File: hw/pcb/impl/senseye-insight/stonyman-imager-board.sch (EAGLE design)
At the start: 10 parts, among them J1 HEADER_12PIN2X6_NOSILK, U1 STONYMANDEFAULT_LENS_MOUNT, U2 TI_ADCXX1S101

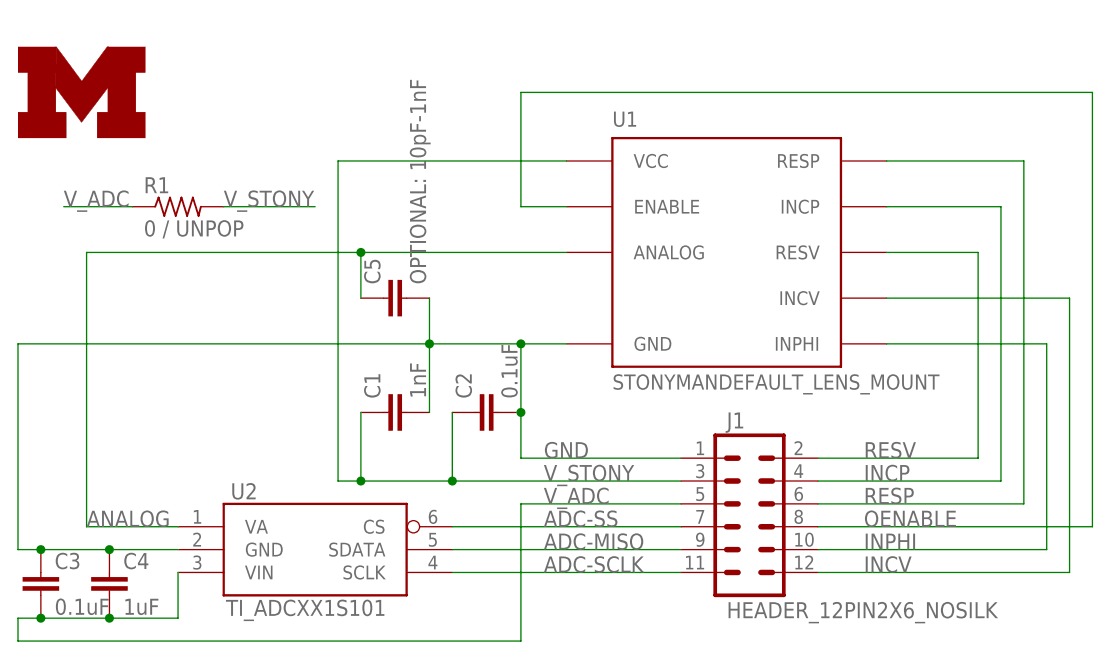
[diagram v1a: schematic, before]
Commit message: fixed ADC pin swap bug in stonyman-imager-board
I had switched pin 1 with pin 3, the positive supply and analog in pins
respectively, due to their stupid names.  I have updated the part so
that the names are very clear now, and also fixed the schematic and
board.
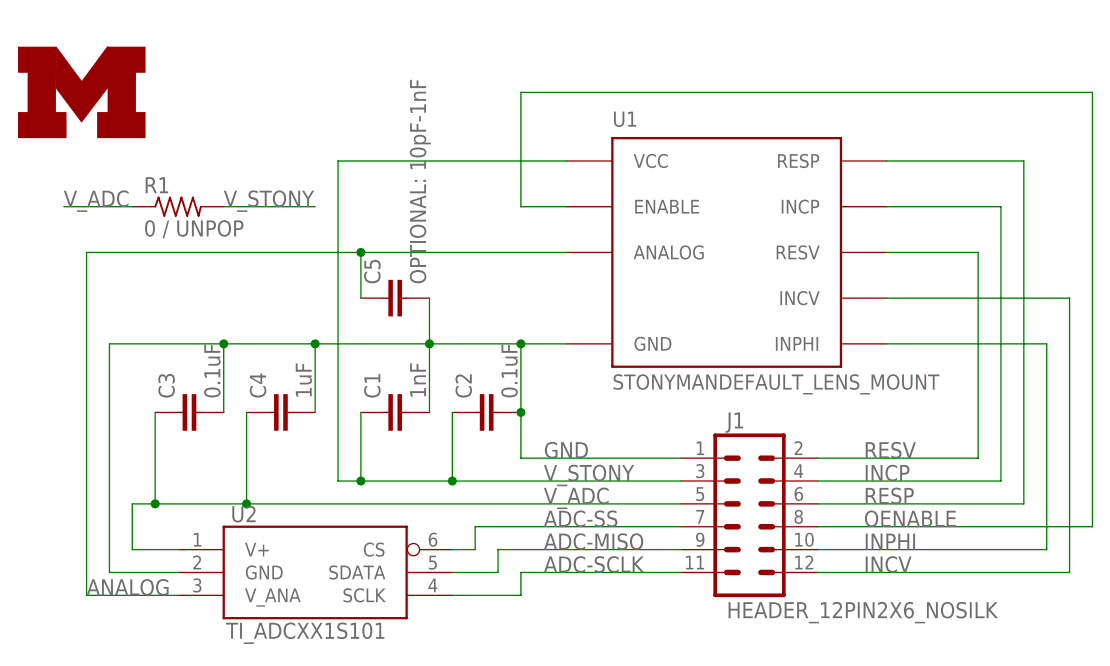
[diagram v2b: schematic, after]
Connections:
- net ANALOG: now also U2.V_ANA; no longer U2.VA
- net GND: now also C3.2, C4.2; no longer C3.1, C4.1
- net V_ADC: now also C3.1, C4.1, U2.V+; no longer C3.2, C4.2, U2.VIN
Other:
- moved on the sheet: C3, C4, U2
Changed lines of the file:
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@@
 </plain>
 <instances>
-<instance part="U2" gate="G$1" x="58.42" y="2.54"/>
+<instance part="U2" gate="G$1" x="58.42" y="0"/>
 <instance part="C1" gate="G$1" x="66.04" y="17.78" rot="R90"/>
 <instance part="C2" gate="G$1" x="76.2" y="17.78" rot="R90"/>
-<instance part="C3" gate="G$1" x="27.94" y="0"/>
-<instance part="C4" gate="G$1" x="35.56" y="0"/>
+<instance part="C3" gate="G$1" x="43.18" y="17.78" rot="R90"/>
+<instance part="C4" gate="G$1" x="53.34" y="17.78" rot="R90"/>
 <instance part="R1" gate="G$1" x="43.18" y="40.64"/>
 <instance part="U1" gate="G$1" x="104.14" y="35.56"/>
@@
 <net name="GND" class="0">
 <segment>
-<wire x1="25.4" y1="25.4" x2="71.12" y2="25.4" width="0.1524" layer="91"/>
+<wire x1="35.56" y1="25.4" x2="48.26" y2="25.4" width="0.1524" layer="91"/>
+<wire x1="48.26" y1="25.4" x2="58.42" y2="25.4" width="0.1524" layer="91"/>
+<wire x1="58.42" y1="25.4" x2="71.12" y2="25.4" width="0.1524" layer="91"/>
 <wire x1="71.12" y1="25.4" x2="81.28" y2="25.4" width="0.1524" layer="91"/>
-<wire x1="25.4" y1="2.54" x2="25.4" y2="25.4" width="0.1524" layer="91"/>
-<pinref part="C3" gate="G$1" pin="1"/>
-<wire x1="25.4" y1="2.54" x2="27.94" y2="2.54" width="0.1524" layer="91"/>
-<pinref part="C4" gate="G$1" pin="1"/>
-<wire x1="27.94" y1="2.54" x2="35.56" y2="2.54" width="0.1524" layer="91"/>
-<junction x="27.94" y="2.54"/>
-<wire x1="35.56" y1="2.54" x2="43.18" y2="2.54" width="0.1524" layer="91"/>
-<junction x="35.56" y="2.54"/>
-<pinref part="U2" gate="G$1" pin="GND"/>
 <pinref part="U1" gate="G$1" pin="GND"/>
 <wire x1="81.28" y1="25.4" x2="86.36" y2="25.4" width="0.1524" layer="91"/>
@@
 <pinref part="C5" gate="G$1" pin="2"/>
 <wire x1="71.12" y1="30.48" x2="71.12" y2="25.4" width="0.1524" layer="91"/>
+<wire x1="35.56" y1="25.4" x2="35.56" y2="0" width="0.1524" layer="91"/>
+<pinref part="U2" gate="G$1" pin="GND"/>
+<wire x1="35.56" y1="0" x2="43.18" y2="0" width="0.1524" layer="91"/>
+<pinref part="C3" gate="G$1" pin="2"/>
+<wire x1="48.26" y1="17.78" x2="48.26" y2="25.4" width="0.1524" layer="91"/>
+<junction x="48.26" y="25.4"/>
+<pinref part="C4" gate="G$1" pin="2"/>
+<wire x1="58.42" y1="17.78" x2="58.42" y2="25.4" width="0.1524" layer="91"/>
+<junction x="58.42" y="25.4"/>
 </segment>
 </net>
@@
 <net name="V_ADC" class="0">
 <segment>
-<label x="83.82" y="7.62" size="1.778" layer="95"/>
-<pinref part="C3" gate="G$1" pin="2"/>
-<wire x1="25.4" y1="-5.08" x2="27.94" y2="-5.08" width="0.1524" layer="91"/>
-<pinref part="C4" gate="G$1" pin="2"/>
-<wire x1="27.94" y1="-5.08" x2="35.56" y2="-5.08" width="0.1524" layer="91"/>
-<junction x="27.94" y="-5.08"/>
-<pinref part="U2" gate="G$1" pin="VIN"/>
-<wire x1="35.56" y1="-5.08" x2="43.18" y2="-5.08" width="0.1524" layer="91"/>
-<wire x1="43.18" y1="-5.08" x2="43.18" y2="0" width="0.1524" layer="91"/>
-<junction x="35.56" y="-5.08"/>
-<wire x1="99.06" y1="7.62" x2="81.28" y2="7.62" width="0.1524" layer="91"/>
-<wire x1="81.28" y1="7.62" x2="81.28" y2="-7.62" width="0.1524" layer="91"/>
-<wire x1="81.28" y1="-7.62" x2="25.4" y2="-7.62" width="0.1524" layer="91"/>
-<wire x1="25.4" y1="-7.62" x2="25.4" y2="-5.08" width="0.1524" layer="91"/>
-<pinref part="J1" gate="G$1" pin="5"/>
-</segment>
-<segment>
 <pinref part="R1" gate="G$1" pin="1"/>
 <wire x1="38.1" y1="40.64" x2="30.48" y2="40.64" width="0.1524" layer="91"/>
 <label x="30.48" y="40.64" size="1.778" layer="95"/>
 </segment>
+<segment>
+<pinref part="J1" gate="G$1" pin="5"/>
+<label x="83.82" y="7.62" size="1.778" layer="95"/>
+<wire x1="99.06" y1="7.62" x2="50.8" y2="7.62" width="0.1524" layer="91"/>
+<wire x1="50.8" y1="7.62" x2="40.64" y2="7.62" width="0.1524" layer="91"/>
+<wire x1="40.64" y1="7.62" x2="38.1" y2="7.62" width="0.1524" layer="91"/>
+<wire x1="38.1" y1="7.62" x2="38.1" y2="2.54" width="0.1524" layer="91"/>
+<pinref part="U2" gate="G$1" pin="V+"/>
+<wire x1="38.1" y1="2.54" x2="43.18" y2="2.54" width="0.1524" layer="91"/>
+<pinref part="C3" gate="G$1" pin="1"/>
+<wire x1="40.64" y1="17.78" x2="40.64" y2="7.62" width="0.1524" layer="91"/>
+<junction x="40.64" y="7.62"/>
+<pinref part="C4" gate="G$1" pin="1"/>
+<wire x1="50.8" y1="17.78" x2="50.8" y2="7.62" width="0.1524" layer="91"/>
+<junction x="50.8" y="7.62"/>
+</segment>
 </net>
 <net name="ANALOG" class="0">
 <segment>
-<pinref part="U2" gate="G$1" pin="VA"/>
-<wire x1="43.18" y1="5.08" x2="33.02" y2="5.08" width="0.1524" layer="91"/>
-<label x="33.02" y="5.08" size="1.778" layer="95"/>
-<wire x1="33.02" y1="5.08" x2="33.02" y2="35.56" width="0.1524" layer="91"/>
+<label x="33.02" y="-2.54" size="1.778" layer="95"/>
+<wire x1="33.02" y1="-2.54" x2="33.02" y2="35.56" width="0.1524" layer="91"/>
 <pinref part="U1" gate="G$1" pin="ANALOG"/>
 <wire x1="33.02" y1="35.56" x2="63.5" y2="35.56" width="0.1524" layer="91"/>
@@
 <wire x1="63.5" y1="30.48" x2="63.5" y2="35.56" width="0.1524" layer="91"/>
 <junction x="63.5" y="35.56"/>
+<pinref part="U2" gate="G$1" pin="V_ANA"/>
+<wire x1="33.02" y1="-2.54" x2="43.18" y2="-2.54" width="0.1524" layer="91"/>
 </segment>
 </net>
@@
 <pinref part="J1" gate="G$1" pin="9"/>
 <pinref part="U2" gate="G$1" pin="SDATA"/>
-<wire x1="73.66" y1="2.54" x2="99.06" y2="2.54" width="0.1524" layer="91"/>
+<wire x1="99.06" y1="2.54" x2="78.74" y2="2.54" width="0.1524" layer="91"/>
+<wire x1="78.74" y1="2.54" x2="78.74" y2="0" width="0.1524" layer="91"/>
+<wire x1="78.74" y1="0" x2="73.66" y2="0" width="0.1524" layer="91"/>
 </segment>
 </net>
@@
 <pinref part="U2" gate="G$1" pin="SCLK"/>
 <pinref part="J1" gate="G$1" pin="11"/>
-<wire x1="73.66" y1="0" x2="99.06" y2="0" width="0.1524" layer="91"/>
+<wire x1="99.06" y1="0" x2="81.28" y2="0" width="0.1524" layer="91"/>
+<wire x1="81.28" y1="0" x2="81.28" y2="-2.54" width="0.1524" layer="91"/>
+<wire x1="81.28" y1="-2.54" x2="73.66" y2="-2.54" width="0.1524" layer="91"/>
 </segment>
 </net>
@@
 <segment>
 <pinref part="U2" gate="G$1" pin="CS"/>
-<wire x1="99.06" y1="5.08" x2="73.66" y2="5.08" width="0.1524" layer="91"/>
 <label x="83.82" y="5.08" size="1.778" layer="95"/>
 <pinref part="J1" gate="G$1" pin="7"/>
-</segment>
-</net>
+<wire x1="99.06" y1="5.08" x2="76.2" y2="5.08" width="0.1524" layer="91"/>
+<wire x1="76.2" y1="5.08" x2="76.2" y2="2.54" width="0.1524" layer="91"/>
+<wire x1="76.2" y1="2.54" x2="73.66" y2="2.54" width="0.1524" layer="91"/>
+</segment>
+</net>
